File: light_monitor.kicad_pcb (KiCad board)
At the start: 2 copper layers, 32.9 x 32.9 mm, 33 parts, among them IC1 TSL25911FN, J1 Conn_01x04_Male, J2 Conn_01x03_Male, J3 USB_B_Micro, U1 STM32L432KCUx, U2 STDC14, U3 TPS610986, U4 LDK130PU33R_DFN6, U5 RV-8803-C7, X1 board_lens

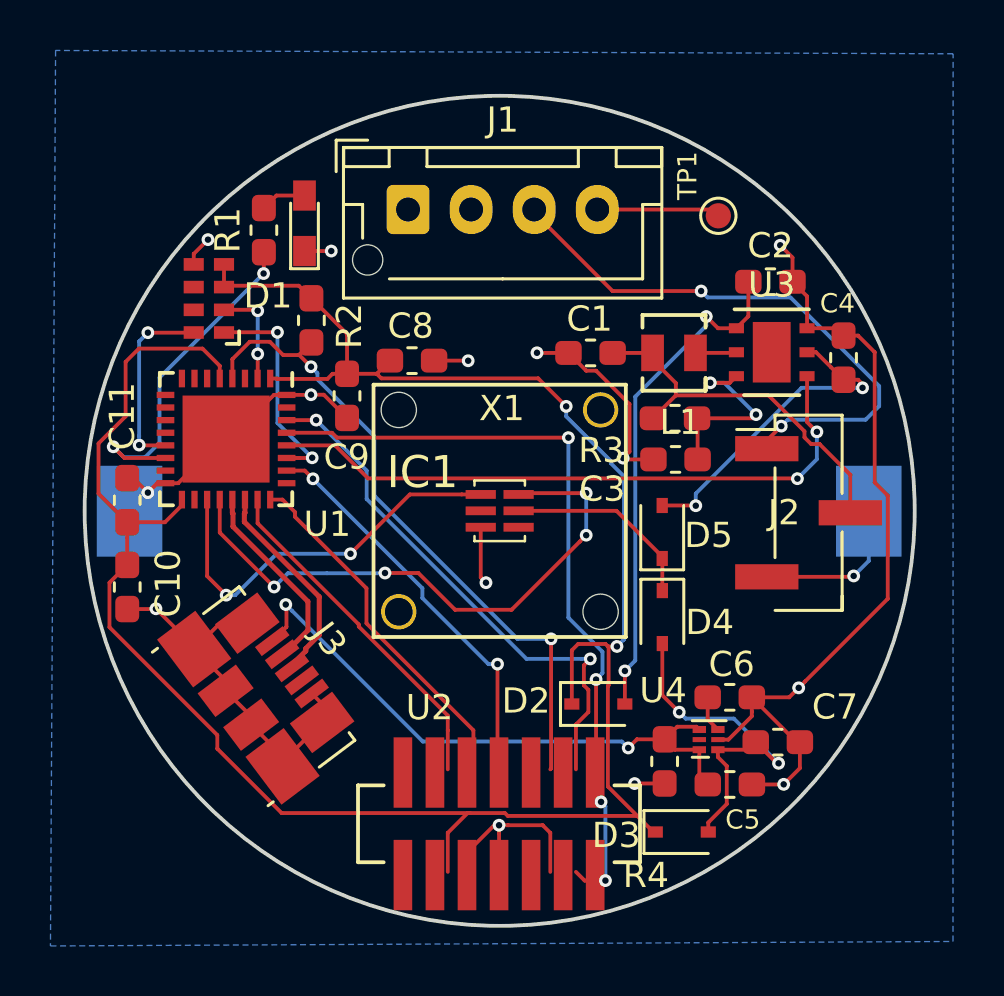
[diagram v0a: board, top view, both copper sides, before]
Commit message: beginning the process of cleaning up the pad issues
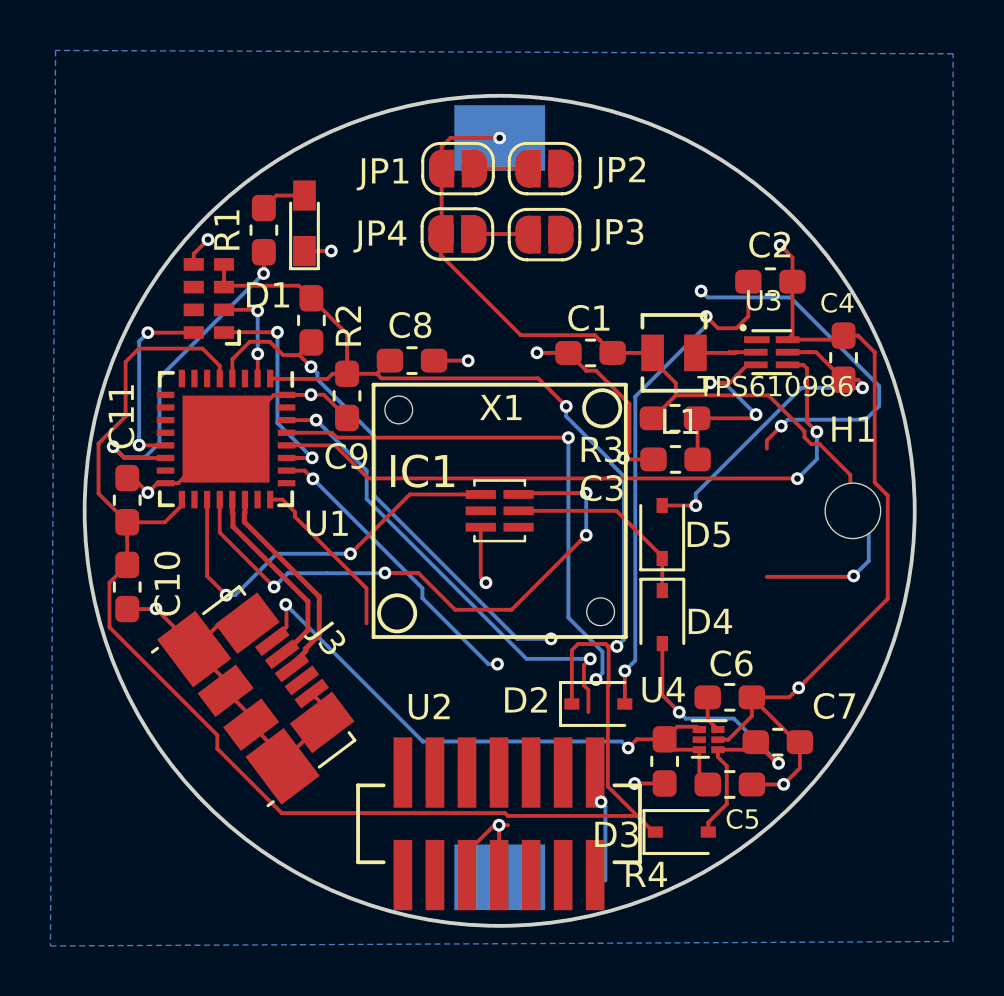
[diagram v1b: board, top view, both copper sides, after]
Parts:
- removed J1: Conn_01x04_Male, Connector_JST:JST_XH_B4B-XH-AM_1x04_P2.50mm_Vertical
- removed J2: Conn_01x03_Male, Connector_PinHeader_2.54mm:PinHeader_1x03_P2.54mm_Vertical_SMD_Pin1Left
- removed TP1: VOUT_MON, TestPoint:TestPoint_Pad_D1.0mm
- added H1: MountingHole, MountingHole:MountingHole_2.2mm_M2, F.Cu at (127.4, 105.2)
- added JP1: Jumper_2_Open, Jumper:SolderJumper-2_P1.3mm_Open_RoundedPad1.0x1.5mm, F.Cu at (111.7, 91.7)
- added JP2: Jumper_2_Open, Jumper:SolderJumper-2_P1.3mm_Open_RoundedPad1.0x1.5mm, F.Cu at (115.1, 91.7)
- added JP3: Jumper_2_Open, Jumper:SolderJumper-2_P1.3mm_Open_RoundedPad1.0x1.5mm, F.Cu at (115.1, 94.3)
- added JP4: Jumper_2_Open, Jumper:SolderJumper-2_P1.3mm_Open_RoundedPad1.0x1.5mm, F.Cu at (111.7, 94.3)
- U3: footprint Package_SON:Texas_PWSON-N6 -> SON50P150X150X80-6N:SON50P150X150X80-6N
- moved BT1 0.14 mm to (113.4, 105.1), turned to 270 degrees
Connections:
- BT1 pad 1: Net-(BT1-Pad1) -> /VBATT
- C1 pad 1: Net-(C1-Pad1) -> /VBATT
- D5 pad 2: Net-(C4-Pad1) -> Net-(D5-Pad2)
- L1 pad 2: Net-(C1-Pad1) -> /VBATT
- R3 pad 1: Net-(C1-Pad1) -> /VBATT
- U1 pad 31: Net-(U1-Pad31) -> VDD
- U3 pad 1: +3V3 -> Net-(JP2-Pad2)
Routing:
- net /VBATT: track 0.00 -> 30.0 mm, vias 0 -> 1
- net Net-(C1-Pad1): track 14.8 -> 0.00 mm
- net /SWDIO: track 13.8 -> 0.00 mm
- net /TX: track 30.9 -> 21.5 mm, vias 4 -> 2
- net Net-(J1-Pad3): track 22.8 -> 14.8 mm
- net /SWDCLK: track 14.3 -> 6.77 mm
- net /NRST: track 26.0 -> 20.8 mm
- net Net-(J1-Pad4): track 4.90 -> 0.00 mm
- net /SWO: track 16.0 -> 11.9 mm
- net VDD: track 90.3 -> 87.7 mm
- net GND: track 84.5 -> 82.2 mm
- net Net-(D5-Pad2): track 0.00 -> 2.16 mm
- net +3V3: track 20.1 -> 22.2 mm
- net /RX: track 21.4 -> 22.7 mm, vias 2 -> 3
- net /SW_MODE: track 25.3 -> 26.5 mm
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
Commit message: completed r002 board - shipped
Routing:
- net GND: track 82.2 -> 99.7 mm
- net Net-(D5-Pad2): track 2.16 -> 17.2 mm, vias 0 -> 2
- net Net-(J1-Pad3): track 14.8 -> 0.00 mm, vias 2 -> 0
- net /SWDIO: track 0.00 -> 13.7 mm
- net Net-(JP2-Pad2): track 0.00 -> 12.2 mm, vias 0 -> 2
- net /TX: track 21.5 -> 32.3 mm, vias 2 -> 3
- net /VBATT: track 30.0 -> 20.1 mm
- net VDD: track 87.7 -> 77.9 mm, vias 2 -> 4
- net +3V3: track 22.2 -> 31.8 mm
- net /SWDCLK: track 6.77 -> 14.3 mm
- net Net-(BT1-Pad1): track 6.27 -> 0.00 mm, vias 1 -> 0
- net /NRST: track 20.8 -> 25.9 mm
- net Net-(C4-Pad1): track 14.0 -> 18.3 mm
- net /SWO: track 11.9 -> 16.1 mm
- net /RX: track 22.7 -> 21.5 mm, vias 3 -> 2
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- added copper zone on F.Cu, net VDD
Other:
- board text added: "R002"

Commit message: sensor complete
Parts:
- removed C2, C5: 10uF, Capacitor_SMD:C_0603_1608Metric_Pad1.05x0.95mm_HandSolder
- removed C3: 0.1uF, Capacitor_SMD:C_0603_1608Metric_Pad1.05x0.95mm_HandSolder
- removed C4, C7: 1uF, Capacitor_SMD:C_0603_1608Metric_Pad1.05x0.95mm_HandSolder
- removed C6: 10nF, Capacitor_SMD:C_0603_1608Metric_Pad1.05x0.95mm_HandSolder
- removed D2, D3, D4, D5: D_Schottky, Diode_SMD:D_SOD-323
- removed H1: MountingHole, MountingHole:MountingHole_2.2mm_M2
- removed J3: USB_B_Micro, Connector_USB:USB_Micro-B_Molex_47346-0001
- removed JP1, JP2, JP3, JP4: Jumper_2_Open, Jumper:SolderJumper-2_P1.3mm_Open_RoundedPad1.0x1.5mm
- removed L1: 4.7uH, bhimebau_inductor:TDKVLF3025
- removed R3: 400, Resistor_SMD:R_0603_1608Metric_Pad1.05x0.95mm_HandSolder
- removed R4: 100k, Resistor_SMD:R_0603_1608Metric_Pad1.05x0.95mm_HandSolder
- removed U3: TPS610986, SON50P150X150X80-6N:SON50P150X150X80-6N
- removed U4: LDK130PU33R_DFN6, Package_DFN_QFN:DFN-6_1.3x1.2mm_P0.4mm
- added G***: LOGO, boardlogo:us_forest_service_logo, F.Cu at (123.8, 105.3)
- added G***: LOGO, boardlogo:board_logo, F.Cu at (108.4, 115.4)
- U2: moved to B.Cu
- moved U2 17.2 mm to (125.4, 105.4), turned to 90 degrees
- moved C1 7.42 mm to (112.4, 93.1)
- moved C9 3.99 mm to (109.9, 97.7), turned to 0 degrees
- moved C11 1.98 mm to (99.8, 106.4), turned to 0 degrees
- moved C10 1.19 mm to (99.8, 108.0), turned to 0 degrees
- moved BT1 0.27 mm to (113.1, 105.2)
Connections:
- BT1 pad 1: /VBATT -> VDD
- C1 pad 1: /VBATT -> VDD
- IC1 pad 2: Net-(IC1-Pad2) -> /sensor_int
- IC1 pad 4: Net-(IC1-Pad4) -> (no net)
- IC1 pad 5: +VSW -> VDD
- U1 pad 10: Net-(U1-Pad10) -> (no net)
- U1 pad 11: Net-(U1-Pad11) -> /rtc_EVI
- U1 pad 12: Net-(U1-Pad12) -> /rtc_nINT
- U1 pad 15: Net-(U1-Pad15) -> (no net)
- U1 pad 18: Net-(U1-Pad18) -> /sensor_int
- U1 pad 21: /USB_N -> (no net)
- U1 pad 22: /USB_P -> (no net)
- U1 pad 25: Net-(U1-Pad25) -> (no net)
- U1 pad 28: /SW_MODE -> (no net)
- U1 pad 29: /TX -> (no net)
- U1 pad 3: Net-(U1-Pad3) -> (no net)
- U1 pad 30: /RX -> (no net)
- U1 pad 31: VDD -> GND
- U1 pad 6: Net-(U1-Pad6) -> (no net)
- U1 pad 7: Net-(U1-Pad7) -> (no net)
- U1 pad 8: Net-(U1-Pad8) -> /TX
- U1 pad 9: Net-(U1-Pad9) -> /RX
- U2 pad 1: Net-(U2-Pad1) -> (no net)
- U2 pad 10: Net-(U2-Pad10) -> (no net)
- U2 pad 13: /TX -> /RX
- U2 pad 14: /RX -> /TX
- U2 pad 2: Net-(U2-Pad2) -> (no net)
- U2 pad 9: Net-(U2-Pad9) -> (no net)
- U5 pad 6: Net-(U5-Pad6) -> /rtc_nINT
- U5 pad 7: Net-(U5-Pad7) -> /rtc_EVI
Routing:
- net GND: track 99.7 -> 30.8 mm, vias 14 -> 10
- net VDD: track 77.9 -> 28.3 mm, vias 4 -> 11
- net +3V3: track 31.8 -> 0.00 mm, vias 2 -> 0
- net Net-(R1-Pad1): track 13.8 -> 41.5 mm, vias 2 -> 4
- net /SW_MODE: track 26.6 -> 0.00 mm, vias 2 -> 0
- net Net-(C5-Pad1): track 23.9 -> 0.00 mm, vias 2 -> 0
- net /SWO: track 16.1 -> 37.0 mm, vias 2 -> 3
- net /SWDCLK: track 14.3 -> 34.5 mm, vias 0 -> 3
- net /VBATT: track 20.1 -> 0.00 mm, vias 1 -> 0
- net /SWDIO: track 13.7 -> 33.7 mm, vias 0 -> 3
- net Net-(C4-Pad1): track 18.3 -> 0.00 mm, vias 2 -> 0
- net Net-(D5-Pad2): track 17.2 -> 0.00 mm, vias 2 -> 0
- net Net-(C7-Pad1): track 14.4 -> 0.00 mm, vias 2 -> 0
- net /sensor_int: track 0.00 -> 12.5 mm, vias 0 -> 2
- net Net-(JP2-Pad2): track 12.2 -> 0.00 mm, vias 2 -> 0
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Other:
- board text added: "Dark Sky"
- board text added: "Light Sensor"
- board text added: "R003"
- board text removed: "R002"

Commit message: checking rev 4
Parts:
- removed G***: LOGO, boardlogo:us_forest_service_logo
- removed G***: LOGO, boardlogo:board_logo
- added C2: 0.1uF, Capacitor_SMD:C_0603_1608Metric_Pad1.05x0.95mm_HandSolder, F.Cu at (115.3, 99.1)
- BT1: footprint Battery:BatteryHolder_Keystone_1060_1x2032 -> bhimebau_battery:Keystone_1091TR
- U2: moved to F.Cu
- moved BT1 31.6 mm to (144.5, 109.0), turned to 180 degrees
- moved U2 16.6 mm to (113.3, 116.7), turned to 0 degrees
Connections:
- IC1 pad 5: VDD -> /sensor_power
- U1 pad 21: (no net) -> /sensor_power
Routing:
- net /SWDCLK: track 34.5 -> 13.2 mm, vias 3 -> 1
- net /sensor_data: track 18.7 -> 5.10 mm, vias 2 -> 1
- net /SWO: track 37.0 -> 28.0 mm, vias 3 -> 2
- net /sensor_int: track 12.5 -> 3.72 mm, vias 2 -> 1
- net VDD: track 28.3 -> 21.3 mm, vias 11 -> 7
- net /TX: track 27.9 -> 23.8 mm
- net /sensor_power: track 0.00 -> 2.54 mm, vias 0 -> 2
- net /RX: track 24.3 -> 22.7 mm
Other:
- board text added: "R004"
- board text removed: "R003"

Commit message: r004 board added
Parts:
- added G***: LOGO, logo:iu_trident, F.Cu at (104.2, 113.2)
- added G***: LOGO, logo:hnf_logo, F.Cu at (123.0, 99.4)
- moved BT1 31.3 mm to (113.2, 107.1)
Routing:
- net /sensor_power: track 2.54 -> 25.8 mm, vias 2 -> 4
- net /RX: track 22.7 -> 40.8 mm, vias 1 -> 2
- net /SWDIO: track 33.7 -> 16.8 mm, vias 3 -> 2
- net GND: track 30.8 -> 45.8 mm, vias 10 -> 11
- net /sensor_data: track 5.10 -> 19.0 mm, vias 1 -> 2
- net /TX: track 23.8 -> 35.8 mm, vias 1 -> 2
- net /SWO: track 28.0 -> 18.6 mm
- net /sensor_int: track 3.72 -> 12.2 mm, vias 1 -> 2
- net VDD: track 21.3 -> 29.0 mm, vias 7 -> 9
- net /SWDCLK: track 13.2 -> 17.3 mm, vias 1 -> 2
- net /NRST: track 29.2 -> 30.2 mm, vias 5 -> 4
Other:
- board size 32.9 x 32.9 mm -> 33.8 x 33.8 mm
- board text added: "Sensor"
- board text removed: "Light Sensor"

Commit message: rev 005 lpuart sent to macrofab
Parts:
- removed G***: LOGO, logo:iu_trident
- removed G***: LOGO, logo:hnf_logo
- removed X1: board_lens, bhimebau_inductor:carclo_lens
- added G30: LOGO, logo:hnf_logo, F.Cu at (121.6, 97.4)
- added G31: LOGO, logo:iu_trident, F.Cu at (104.0, 113.3)
- added J1: Conn_01x03, Connector_JST:JST_XH_B3B-XH-AM_1x03_P2.50mm_Vertical, F.Cu at (124.7, 105.4)
- added R3: 200, Resistor_SMD:R_0603_1608Metric_Pad1.05x0.95mm_HandSolder, F.Cu at (120.5, 114.7)
- added R4: 200, Resistor_SMD:R_0603_1608Metric_Pad1.05x0.95mm_HandSolder, F.Cu at (120.5, 116.6)
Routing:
- net Net-(J1-Pad1): track 0.00 -> 10.8 mm
- net Net-(J1-Pad2): track 0.00 -> 10.1 mm
- net /TX: track 35.8 -> 38.4 mm
- net /RX: track 40.8 -> 43.1 mm
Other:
- board text added: "R005-LU"
- board text removed: "R004"
- board text removed: "Sensor"

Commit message: r006 sensor committed
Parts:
- removed C1: 10uF, Capacitor_SMD:C_0603_1608Metric_Pad1.05x0.95mm_HandSolder
- removed C2: 0.1uF, Capacitor_SMD:C_0603_1608Metric_Pad1.05x0.95mm_HandSolder
- removed G30: LOGO, logo:hnf_logo
- removed G31: LOGO, logo:iu_trident
- removed R2: 100k, Resistor_SMD:R_0603_1608Metric_Pad1.05x0.95mm_HandSolder
- added G***: LOGO, logo:iu_trident, F.Cu at (113.5, 123.8)
- added G***: LOGO, logo:hnf_logo, F.Cu at (113.0, 86.5)
- added IC2: TSL237S-LF, SamacSys_Parts_3:TSL237S-LF, F.Cu at (113.3, 101.2)
- added U3: sm_tsl237, bhimebau_lightsensor:tsl237t, F.Cu at (119.8, 102.5)
- J1, U2: moved to B.Cu
- moved D1 15.3 mm to (93.6, 103.3)
- moved R1 15.3 mm to (92.0, 103.6)
- moved U2 14.8 mm to (98.5, 116.8), turned to 132 degrees
- moved J1 9.62 mm to (130.1, 113.3), turned to 230 degrees
- moved IC1 5.41 mm to (108.0, 105.3)
- moved C10 4.28 mm to (96.8, 105.0), turned to 90 degrees
- moved C8 4.07 mm to (105.9, 98.5)
- moved C9 4.07 mm to (105.9, 96.9)
- moved U5 3.47 mm to (99.2, 94.5)
- moved R4 3.11 mm to (120.9, 113.5)
- moved R3 2.94 mm to (120.8, 111.8)
- moved C11 1.81 mm to (98.5, 105.1), turned to 90 degrees
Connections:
- U1 pad 10: (no net) -> /tsl237_pwr
- U1 pad 11: /rtc_EVI -> /tsl237_freq
- U1 pad 3: (no net) -> /rtc_EVI
- U1 pad 6: (no net) -> /sm_237t_pwr
- U1 pad 7: (no net) -> /sm_237t_freq
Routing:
- net Net-(R1-Pad1): track 41.5 -> 13.0 mm
- net /sm_237t_pwr: track 0.00 -> 27.0 mm, vias 0 -> 2
- net /sm_237t_freq: track 0.00 -> 26.2 mm, vias 0 -> 2
- net /TX: track 38.4 -> 57.4 mm, vias 2 -> 6
- net /tsl237_pwr: track 0.00 -> 17.9 mm, vias 0 -> 1
- net GND: track 45.8 -> 29.4 mm, vias 11 -> 6
- net /tsl237_freq: track 0.00 -> 16.0 mm, vias 0 -> 1
- net /sensor_power: track 25.8 -> 14.6 mm, vias 4 -> 2
- net /RX: track 43.1 -> 53.9 mm, vias 2 -> 5
- net /SWO: track 18.6 -> 27.2 mm, vias 2 -> 3
- net /NRST: track 30.2 -> 38.6 mm, vias 4 -> 3
- net /rtc_EVI: track 6.68 -> 12.6 mm, vias 0 -> 2
- net /rtc_data: track 11.8 -> 17.4 mm
- net /rtc_nINT: track 8.22 -> 13.6 mm, vias 0 -> 2
- net /oscillator: track 3.85 -> 8.47 mm
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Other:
- board size 33.8 x 33.8 mm -> 50.2 x 50.2 mm
- board text added: "R006"
- board text removed: "R005-LU"

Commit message: checkin for rev 6
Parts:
- added J2: Conn_01x04_Male, Connector_JST:JST_XH_B4B-XH-AM_1x04_P2.50mm_Vertical, B.Cu at (116.3, 124.0)
- added J3: Conn_01x03_Male, Connector_PinHeader_2.54mm:PinHeader_1x03_P2.54mm_Vertical, B.Cu at (121.3, 126.1)
- added J4: Conn_01x02_Male, Connector_PinHeader_2.54mm:PinHeader_1x02_P2.54mm_Vertical, F.Cu at (119.8, 109.2)
- added J5: Conn_01x03_Male, Connector_PinHeader_2.54mm:PinHeader_1x03_P2.54mm_Vertical, F.Cu at (124.7, 90.2)
- added J6: Conn_01x03_Male, Connector_PinHeader_2.54mm:PinHeader_1x03_P2.54mm_Vertical, F.Cu at (124.8, 100.5)
- added J7: Conn_01x02_Male, Connector_PinHeader_2.54mm:PinHeader_1x02_P2.54mm_Vertical, F.Cu at (103.4, 91.7)
- added J8: Conn_01x07_Male, Connector_PinHeader_2.54mm:PinHeader_1x07_P2.54mm_Vertical, F.Cu at (117.9, 84.3)
- added J9: Conn_01x05_Male, Connector_PinHeader_2.54mm:PinHeader_1x05_P2.54mm_Vertical, F.Cu at (132.3, 96.8)
- moved G*** 27.9 mm to (105.9, 113.5)
- moved G*** 19.6 mm to (96.8, 113.5)
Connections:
- BT1 pad 1: VDD -> Net-(BT1-Pad1)
- C10 pad 1: VDD -> /l432_pwr
- C11 pad 1: VDD -> /l432_pwr
- C8 pad 1: VDD -> /l432_pwr
- C9 pad 1: VDD -> /l432_pwr
- IC1 pad 5: /sensor_power -> /sensor_vdd
- IC2 pad 2: /tsl237_pwr -> /tsl237_vdd
- U1 pad 1: VDD -> /l432_pwr
- U1 pad 17: VDD -> /l432_pwr
- U1 pad 5: VDD -> /l432_pwr
- U3 pad 3: /sm_237t_pwr -> /sm_237t_vdd
- U5 pad 3: VDD -> /rtc_vdd
- U5 pad 4: VDD -> /rtc_vdd
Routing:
- net /l432_pwr: track 0.00 -> 53.1 mm, vias 0 -> 6
- net /rtc_clock: track 10.1 -> 47.1 mm, vias 0 -> 3
- net GND: track 29.4 -> 64.2 mm, vias 6 -> 9
- net /rtc_nINT: track 13.6 -> 45.7 mm, vias 2 -> 7
- net /sensor_clock: track 13.5 -> 45.1 mm, vias 2 -> 6
- net /sensor_int: track 10.7 -> 41.6 mm, vias 2 -> 6
- net /sensor_data: track 18.5 -> 49.0 mm, vias 2 -> 5
- net /sensor_vdd: track 0.00 -> 28.7 mm, vias 0 -> 5
- net /rtc_EVI: track 12.6 -> 37.7 mm, vias 2 -> 5
- net /rtc_vdd: track 0.00 -> 24.9 mm, vias 0 -> 2
- net /tsl237_freq: track 16.0 -> 39.3 mm, vias 1 -> 3
- net /tsl237_vdd: track 0.00 -> 20.5 mm, vias 0 -> 2
- net /rtc_data: track 17.4 -> 36.6 mm, vias 2 -> 3
- net /sensor_power: track 14.6 -> 33.1 mm, vias 2 -> 1
- net /tsl237_pwr: track 17.9 -> 33.4 mm, vias 1 -> 3
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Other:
- board text added: "237"
- board text added: "237t"
- board text added: "25911"
- board text added: "L432"
- board text added: "batt"
- board text added: "board"
- board text added: "clk"
- board text added: "data"
- board text added: "evi"
- board text added: "hz"
- board text added: "in"
- board text added: "int"
- board text added: "mon"
- board text added: "nint"
- board text added: "osc"
- board text added: "pwr"
- board text added: "rtc"
- board text added: "rx"
- board text added: "tx"
